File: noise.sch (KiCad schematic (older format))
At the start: 31 parts, among them U1 4584, U2 TL072, U3 78L05

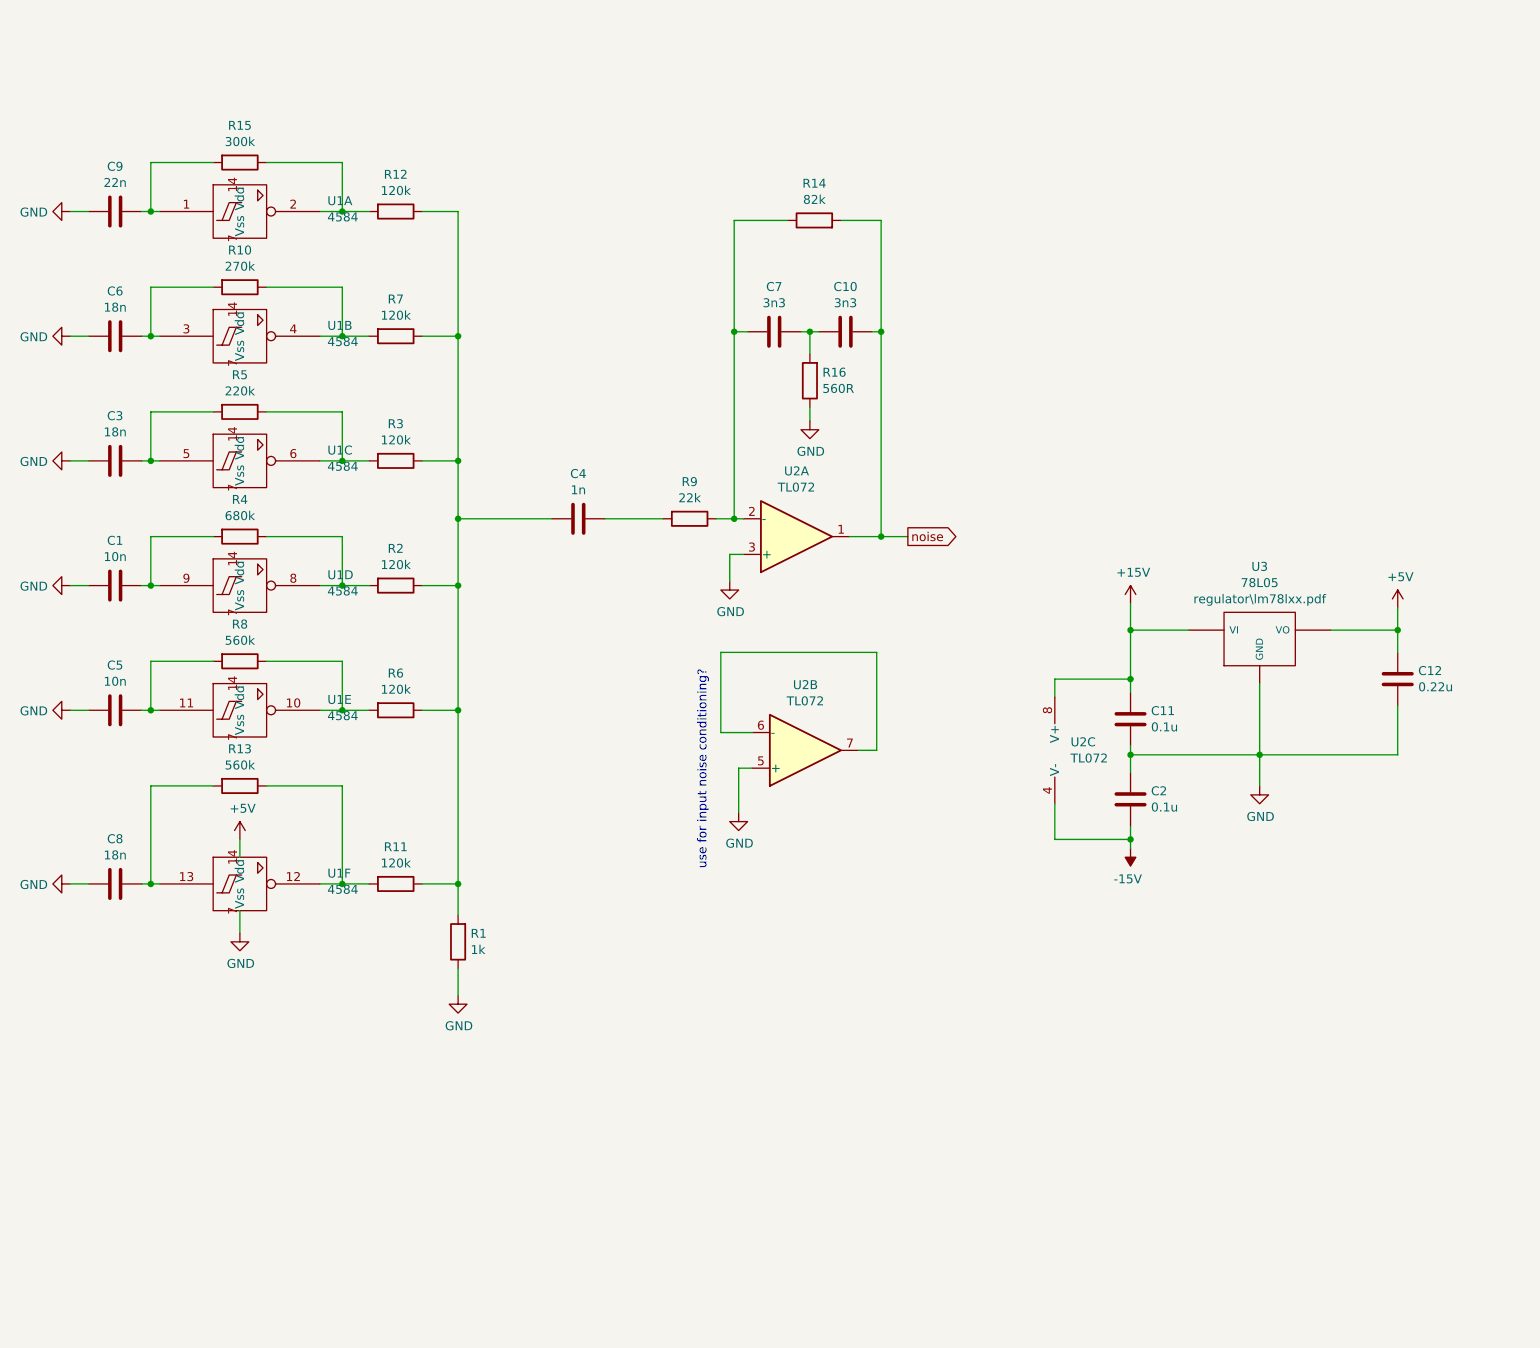
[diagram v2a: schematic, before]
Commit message: fixup noise generator connections
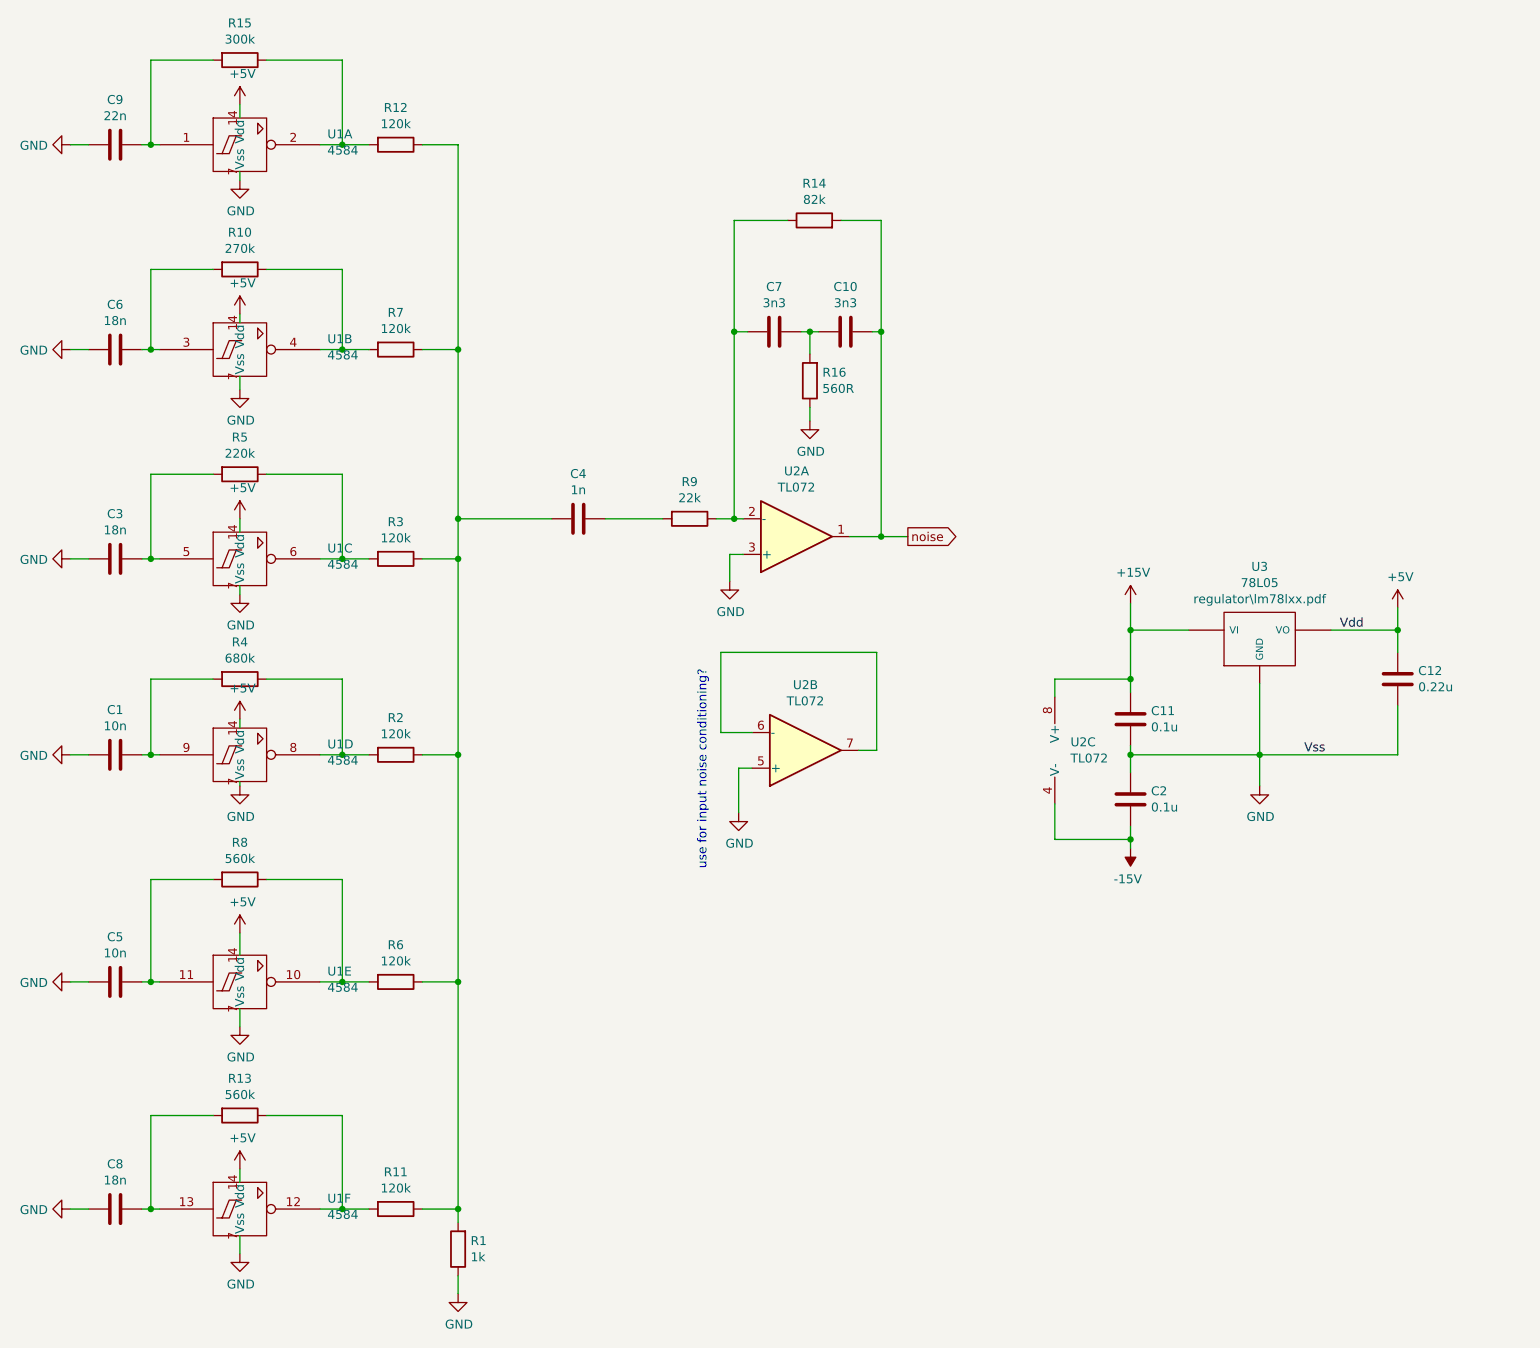
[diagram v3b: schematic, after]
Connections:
- net +5V: now also U1.14 (Vdd), U1.14 (Vdd), U1.14 (Vdd), U1.14 (Vdd), U1.14 (Vdd)
- net GND: now also U1.7 (Vss), U1.7 (Vss), U1.7 (Vss), U1.7 (Vss), U1.7 (Vss)
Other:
- moved on the sheet: C1, C3, C5, C6, C8, C9, R1, R10, R11, R12, R13, R15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

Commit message: noise in/out with selection
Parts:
- added J7: noisesel, symbol Connector:Conn_01x03_Male
- added J8: noisein, symbol Connector:Conn_01x01_Male
- added J9: noiseout, symbol Connector:Conn_01x01_Male
- added R67: 1k, symbol Device:R
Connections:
- net GND: no longer U2.5 (+)
- net noise: now also J7.2 (Pin_2); no longer C10.1, R14.2, U2.1
- net at U2.6 (-), U2.7: now also R67.2
- new net: J9.1 (Pin_1), R67.1
- new net: C10.1, J7.1 (Pin_1), R14.2, U2.1, U2.5 (+)
- new net: J7.3 (Pin_3), J8.1 (Pin_1)
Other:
- note added: "ext noise mod, bridge 1 and 2 of j7 to disable"
- note removed: "use for input noise conditioning?"
- moved on the sheet: U2B
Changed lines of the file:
@@
 Wire Wire Line
 	4100 3300 3775 3300
-Text GLabel 5475 3400 2    50   Output ~ 0
+Text GLabel 6175 3400 2    50   Output ~ 0
 noise
-Wire Wire Line
-	5475 3400 5325 3400
 $Comp
 L Device:C C7
@@
 	4500 3300 4400 3300
 Wire Wire Line
-	5325 2250 5325 3400
+	5325 2250 5325 2700
 Connection ~ 5325 2250
-Connection ~ 5325 3400
 Wire Wire Line
 	5325 3400 5150 3400
@@
 L Amplifier_Operational:TL072 U2
 U 2 1 5CC85CA2
-P 4900 4600
-F 0 "U2" H 4900 4233 50  0000 C CNN
-F 1 "TL072" H 4900 4324 50  0000 C CNN
-F 2 "" H 4900 4600 50  0001 C CNN
-F 3 "http://www.ti.com/lit/ds/symlink/tl071.pdf" H 4900 4600 50  0001 C CNN
-	2    4900 4600
+P 6625 2600
+F 0 "U2" H 6625 2233 50  0000 C CNN
+F 1 "TL072" H 6625 2324 50  0000 C CNN
+F 2 "" H 6625 2600 50  0001 C CNN
+F 3 "http://www.ti.com/lit/ds/symlink/tl071.pdf" H 6625 2600 50  0001 C CNN
+	2    6625 2600
 	1    0    0    1
 $EndComp
 Wire Wire Line
-	4600 4500 4425 4500
-Wire Wire Line
-	4425 4050 5300 4050
-Wire Wire Line
-	5300 4050 5300 4600
-Wire Wire Line
-	5300 4600 5200 4600
-$Comp
-L power:GND #PWR0146
-U 1 1 5CC886A6
-P 4525 4950
-F 0 "#PWR0146" H 4525 4700 50  0001 C CNN
-F 1 "GND" H 4530 4777 50  0000 C CNN
-F 2 "" H 4525 4950 50  0001 C CNN
-F 3 "" H 4525 4950 50  0001 C CNN
-	1    4525 4950
-	1    0    0    -1
-$EndComp
-Wire Wire Line
-	4600 4700 4525 4700
-Wire Wire Line
-	4525 4700 4525 4950
+	6325 2500 6150 2500
+Wire Wire Line
+	6150 2050 7025 2050
+Wire Wire Line
+	7025 2050 7025 2600
+Wire Wire Line
+	7025 2600 6925 2600
 $Comp
 L Amplifier_Operational:TL072 U2
@@
 Connection ~ 2950 2350
 Wire Wire Line
-	4425 4500 4425 4050
-Text Notes 4350 4150 3    50   ~ 0
-use for input noise conditioning?
+	6150 2500 6150 2050
+Wire Wire Line
+	5325 2700 6325 2700
+Connection ~ 5325 2700
+Wire Wire Line
+	5325 2700 5325 3400
+$Comp
+L Device:R R67
+U 1 1 5CB9F9E2
+P 7400 2600
+F 0 "R67" V 7193 2600 50  0000 C CNN
+F 1 "1k" V 7284 2600 50  0000 C CNN
+F 2 "" V 7330 2600 50  0001 C CNN
+F 3 "~" H 7400 2600 50  0001 C CNN
+	1    7400 2600
+	0    1    1    0
+$EndComp
+Wire Wire Line
+	7250 2600 7025 2600
+Connection ~ 7025 2600
+$Comp
+L Connector:Conn_01x01_Male J9
+U 1 1 5CBA38EB
+P 7850 2600
+F 0 "J9" H 7822 2530 50  0000 R CNN
+F 1 "noiseout" H 7822 2621 50  0000 R CNN
+F 2 "" H 7850 2600 50  0001 C CNN
+F 3 "~" H 7850 2600 50  0001 C CNN
+	1    7850 2600
+	-1   0    0    1
+$EndComp
+Wire Wire Line
+	7550 2600 7650 2600
+$Comp
+L Connector:Conn_01x03_Male J7
+U 1 1 5CBAF9DC
+P 5675 3000
+F 0 "J7" V 5735 2812 50  0000 R CNN
+F 1 "noisesel" V 5826 2812 50  0000 R CNN
+F 2 "" H 5675 3000 50  0001 C CNN
+F 3 "~" H 5675 3000 50  0001 C CNN
+	1    5675 3000
+	0    -1   1    0
+$EndComp
+Wire Wire Line
+	5575 3200 5575 3400
+Wire Wire Line
+	5575 3400 5325 3400
+Connection ~ 5325 3400
+Wire Wire Line
+	5675 3200 5675 3400
+Wire Wire Line
+	5675 3400 6175 3400
+$Comp
+L Connector:Conn_01x01_Male J8
+U 1 1 5CBBB5C9
+P 5775 3800
+F 0 "J8" V 5928 3712 50  0000 R CNN
+F 1 "noisein" V 5837 3712 50  0000 R CNN
+F 2 "" H 5775 3800 50  0001 C CNN
+F 3 "~" H 5775 3800 50  0001 C CNN
+	1    5775 3800
+	0    -1   -1   0
+$EndComp
+Wire Wire Line
+	5775 3200 5775 3600
+Text Notes 6375 3025 0    50   ~ 0
+ext noise mod, bridge 1 and 2 of j7 to disable
 $EndSCHEMATC

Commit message: noise mods
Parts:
- added J10: noisepresel, symbol Connector:Conn_01x03_Male
- added J11: noisein-pre, symbol Connector:Conn_01x01_Male
- added J12: noiseoutsrc, symbol Connector:Conn_01x03_Male
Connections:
- net at C10.1, J7.1 (Pin_1), R14.2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: now also J12.3 (Pin_3); no longer U2.5 (+)
- net at R1.2, R11.1, R12.1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: now also J10.1 (Pin_1), J12.1 (Pin_1); no longer C4.2
- new net: J12.2 (Pin_2), U2.5 (+)
- new net: C4.2, J10.2 (Pin_2)
- new net: J10.3 (Pin_3), J11.1 (Pin_1)
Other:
- note added: "to disable noise mod, bridge 1/2 of j10 and 1/2 of j7"
- note added: "unsure if ext noise is better before or after U2A, so providing both\nvia J10 and J7"
- note added: "usure if we'd like output before or after U2A, providing both via J12"
- note removed: "ext noise mod, bridge 1 and 2 of j7 to disable"
- moved on the sheet: J9, R67, U2B
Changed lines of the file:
@@
 Wire Wire Line
 	4500 3300 4400 3300
-Wire Wire Line
-	5325 2250 5325 2700
 Connection ~ 5325 2250
 Wire Wire Line
@@
 L Amplifier_Operational:TL072 U2
 U 2 1 5CC85CA2
-P 6625 2600
-F 0 "U2" H 6625 2233 50  0000 C CNN
-F 1 "TL072" H 6625 2324 50  0000 C CNN
-F 2 "" H 6625 2600 50  0001 C CNN
-F 3 "http://www.ti.com/lit/ds/symlink/tl071.pdf" H 6625 2600 50  0001 C CNN
-	2    6625 2600
+P 5900 1150
+F 0 "U2" H 5900 783 50  0000 C CNN
+F 1 "TL072" H 5900 874 50  0000 C CNN
+F 2 "" H 5900 1150 50  0001 C CNN
+F 3 "http://www.ti.com/lit/ds/symlink/tl071.pdf" H 5900 1150 50  0001 C CNN
+	2    5900 1150
 	1    0    0    1
 $EndComp
 Wire Wire Line
-	6325 2500 6150 2500
-Wire Wire Line
-	6150 2050 7025 2050
-Wire Wire Line
-	7025 2050 7025 2600
-Wire Wire Line
-	7025 2600 6925 2600
+	5600 1050 5425 1050
+Wire Wire Line
+	5425 600  6300 600
+Wire Wire Line
+	6300 600  6300 1150
+Wire Wire Line
+	6300 1150 6200 1150
 $Comp
 L Amplifier_Operational:TL072 U2
@@
 	1725 1350 1725 1400
 Wire Wire Line
-	2950 1200 2950 2350
+	2950 1200 2950 1425
 $Comp
 L power:+5V #PWR0157
@@
 Connection ~ 2950 7175
 Connection ~ 2950 3525
-Wire Wire Line
-	3475 3300 2950 3300
-Wire Wire Line
-	2950 2350 2950 3300
-Connection ~ 2950 3300
-Wire Wire Line
-	2950 3300 2950 3525
 Connection ~ 2950 2350
 Wire Wire Line
-	6150 2500 6150 2050
-Wire Wire Line
-	5325 2700 6325 2700
-Connection ~ 5325 2700
-Wire Wire Line
-	5325 2700 5325 3400
+	5425 1050 5425 600
 $Comp
 L Device:R R67
 U 1 1 5CB9F9E2
-P 7400 2600
-F 0 "R67" V 7193 2600 50  0000 C CNN
-F 1 "1k" V 7284 2600 50  0000 C CNN
-F 2 "" V 7330 2600 50  0001 C CNN
-F 3 "~" H 7400 2600 50  0001 C CNN
-	1    7400 2600
+P 6675 1150
+F 0 "R67" V 6468 1150 50  0000 C CNN
+F 1 "1k" V 6559 1150 50  0000 C CNN
+F 2 "" V 6605 1150 50  0001 C CNN
+F 3 "~" H 6675 1150 50  0001 C CNN
+	1    6675 1150
 	0    1    1    0
 $EndComp
 Wire Wire Line
-	7250 2600 7025 2600
-Connection ~ 7025 2600
+	6525 1150 6300 1150
+Connection ~ 6300 1150
 $Comp
 L Connector:Conn_01x01_Male J9
 U 1 1 5CBA38EB
-P 7850 2600
-F 0 "J9" H 7822 2530 50  0000 R CNN
-F 1 "noiseout" H 7822 2621 50  0000 R CNN
-F 2 "" H 7850 2600 50  0001 C CNN
-F 3 "~" H 7850 2600 50  0001 C CNN
-	1    7850 2600
+P 7125 1150
+F 0 "J9" H 7097 1080 50  0000 R CNN
+F 1 "noiseout" H 7097 1171 50  0000 R CNN
+F 2 "" H 7125 1150 50  0001 C CNN
+F 3 "~" H 7125 1150 50  0001 C CNN
+	1    7125 1150
 	-1   0    0    1
 $EndComp
 Wire Wire Line
-	7550 2600 7650 2600
+	6825 1150 6925 1150
 $Comp
 L Connector:Conn_01x03_Male J7
@@
 Wire Wire Line
 	5775 3200 5775 3600
-Text Notes 6375 3025 0    50   ~ 0
-ext noise mod, bridge 1 and 2 of j7 to disable
+Wire Wire Line
+	5325 2250 5325 3400
+$Comp
+L Connector:Conn_01x03_Male J12
+U 1 1 5CBC56BD
+P 4475 775
+F 0 "J12" V 4535 587 50  0000 R CNN
+F 1 "noiseoutsrc" V 4626 587 50  0000 R CNN
+F 2 "" H 4475 775 50  0001 C CNN
+F 3 "~" H 4475 775 50  0001 C CNN
+	1    4475 775
+	0    -1   1    0
+$EndComp
+Wire Wire Line
+	4475 975  4475 1250
+Wire Wire Line
+	4475 1250 5600 1250
+Wire Wire Line
+	5325 1625 5325 1150
+Wire Wire Line
+	5325 1150 4575 1150
+Wire Wire Line
+	4575 1150 4575 975
+Connection ~ 5325 1625
+Wire Wire Line
+	4375 975  4375 1425
+Wire Wire Line
+	4375 1425 2950 1425
+Connection ~ 2950 1425
+Wire Wire Line
+	2950 1425 2950 2350
+Wire Wire Line
+	2950 2350 2950 3300
+$Comp
+L Connector:Conn_01x03_Male J10
+U 1 1 5CBD301E
+P 3425 3800
+F 0 "J10" V 3578 3613 50  0000 R CNN
+F 1 "noisepresel" V 3487 3613 50  0000 R CNN
+F 2 "" H 3425 3800 50  0001 C CNN
+F 3 "~" H 3425 3800 50  0001 C CNN
+	1    3425 3800
+	0    -1   -1   0
+$EndComp
+Wire Wire Line
+	3475 3300 3425 3300
+Wire Wire Line
+	3425 3300 3425 3600
+Wire Wire Line
+	2950 3300 3325 3300
+Wire Wire Line
+	3325 3300 3325 3600
+Connection ~ 2950 3300
+Wire Wire Line
+	2950 3300 2950 3525
+$Comp
+L Connector:Conn_01x01_Male J11
+U 1 1 5CBE0A5A
+P 3650 4200
+F 0 "J11" V 3803 4113 50  0000 R CNN
+F 1 "noisein-pre" V 3712 4113 50  0000 R CNN
+F 2 "" H 3650 4200 50  0001 C CNN
+F 3 "~" H 3650 4200 50  0001 C CNN
+	1    3650 4200
+	0    -1   -1   0
+$EndComp
+Wire Wire Line
+	3525 3600 3525 3525
+Wire Wire Line
+	3525 3525 3650 3525
+Wire Wire Line
+	3650 3525 3650 4000
+Text Notes 3325 4625 0    50   ~ 0
+unsure if ext noise is better before or after U2A, so providing both\nvia J10 and J7
+Text Notes 5675 1625 0    50   ~ 0
+usure if we'd like output before or after U2A, providing both via J12
+Text Notes 5675 2700 0    50   ~ 0
+to disable noise mod, bridge 1/2 of j10 and 1/2 of j7
 $EndSCHEMATC

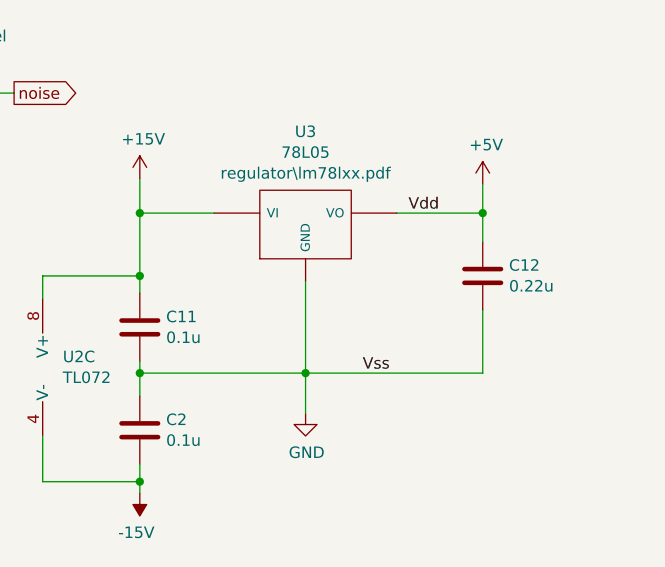
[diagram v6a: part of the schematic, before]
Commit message: removed labels
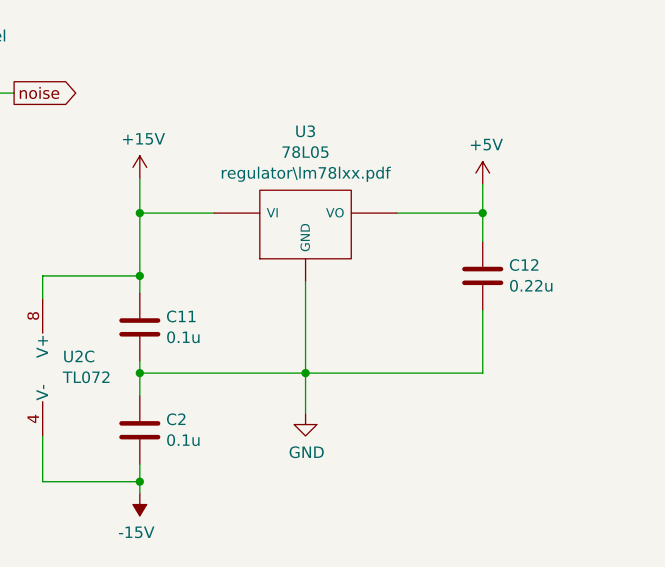
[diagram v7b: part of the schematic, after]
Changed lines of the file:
@@
 	8225 3800 8225 3925
 Connection ~ 8225 3925
-Text Label 7900 3925 0    50   ~ 0
-Vdd
-Text Label 7700 4625 0    50   ~ 0
-Vss
 $Comp
 L power:+5V #PWR0150

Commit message: added hex-inverter style trigger conditioning (amplification?)
https://static1.squarespace.com/static/54c8f37ae4b015761b133d43/550b9d69e4b0c859c95703b9/550b9d69e4b0c859c95703ba/1426824558402/NeinOhNein_KICK_v1_schem.png?format=2500w
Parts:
- removed U2: TL072, symbol Amplifier_Operational:TL072
- added U2: TL074, symbol Amplifier_Operational:TL074
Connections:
- net +15V: now also U2.4 (V+)
- net -15V: now also U2.11 (V-)
- net GND: now also U2.3 (+)
- net at R67.2: now also U2.6 (-), U2.7
- net at C10.1, J12.3 (Pin_3), J7.1 (Pin_1)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: now also U2.1
- net at J12.2 (Pin_2): now also U2.5 (+)
- net at C7.2, R14.1, R9.1: now also U2.2 (-)
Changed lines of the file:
@@
-$EndComp
-$Comp
-L Amplifier_Operational:TL072 U2
-U 1 1 5CC50371
-P 4850 3400
-F 0 "U2" H 4850 3033 50  0000 C CNN
-F 1 "TL072" H 4850 3124 50  0000 C CNN
-F 2 "" H 4850 3400 50  0001 C CNN
-F 3 "http://www.ti.com/lit/ds/symlink/tl071.pdf" H 4850 3400 50  0001 C CNN
-	1    4850 3400
-	1    0    0    1
 $EndComp
 $Comp
@@
 	-1   0    0    1
 $EndComp
-$Comp
-L Amplifier_Operational:TL072 U2
-U 2 1 5CC85CA2
-P 5900 1150
-F 0 "U2" H 5900 783 50  0000 C CNN
-F 1 "TL072" H 5900 874 50  0000 C CNN
-F 2 "" H 5900 1150 50  0001 C CNN
-F 3 "http://www.ti.com/lit/ds/symlink/tl071.pdf" H 5900 1150 50  0001 C CNN
-	2    5900 1150
-	1    0    0    1
-$EndComp
 Wire Wire Line
 	5600 1050 5425 1050
@@
 Wire Wire Line
 	6300 1150 6200 1150
-$Comp
-L Amplifier_Operational:TL072 U2
-U 3 1 5CC8B124
-P 6200 4600
-F 0 "U2" H 6012 4646 50  0000 R CNN
-F 1 "TL072" H 6012 4555 50  0000 R CNN
-F 2 "" H 6200 4600 50  0001 C CNN
-F 3 "http://www.ti.com/lit/ds/symlink/tl071.pdf" H 6200 4600 50  0001 C CNN
-	3    6200 4600
-	-1   0    0    -1
-$EndComp
 Wire Wire Line
 	6725 4200 6300 4200
@@
 Text Notes 5675 2700 0    50   ~ 0
 to disable noise mod, bridge 1/2 of j10 and 1/2 of j7
+$Comp
+L Amplifier_Operational:TL074 U2
+U 1 1 5CE32403
+P 4850 3400
+F 0 "U2" H 4850 3033 50  0000 C CNN
+F 1 "TL074" H 4850 3124 50  0000 C CNN
+F 2 "" H 4800 3500 50  0001 C CNN
+F 3 "http://www.ti.com/lit/ds/symlink/tl071.pdf" H 4900 3600 50  0001 C CNN
+	1    4850 3400
+	1    0    0    1
+$EndComp
+$Comp
+L Amplifier_Operational:TL074 U2
+U 2 1 5CE325FE
+P 5900 1150
+F 0 "U2" H 5900 783 50  0000 C CNN
+F 1 "TL074" H 5900 874 50  0000 C CNN
+F 2 "" H 5850 1250 50  0001 C CNN
+F 3 "http://www.ti.com/lit/ds/symlink/tl071.pdf" H 5950 1350 50  0001 C CNN
+	2    5900 1150
+	1    0    0    1
+$EndComp
+$Comp
+L Amplifier_Operational:TL074 U2
+U 5 1 5CE3374E
+P 6400 4600
+F 0 "U2" H 6358 4646 50  0000 L CNN
+F 1 "TL074" H 6358 4555 50  0000 L CNN
+F 2 "" H 6350 4700 50  0001 C CNN
+F 3 "http://www.ti.com/lit/ds/symlink/tl071.pdf" H 6450 4800 50  0001 C CNN
+	5    6400 4600
+	1    0    0    -1
+$EndComp
 $EndSCHEMATC
